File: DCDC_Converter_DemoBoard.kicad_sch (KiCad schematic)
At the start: 90 parts, among them J1 Conn_01x01, J10 Conn_01x01, J11 Conn_01x01, J12 Conn_01x01, J13 Conn_01x01, J14 Conn_01x01, J15 Conn_01x01, J16 Conn_01x01, J17 Conn_01x01, J18 Conn_01x01, J19 Conn_01x01, J2 Conn_01x01, J20 Conn_01x01, J21 Conn_01x01, J22 Conn_01x01, J23 Conn_01x01, J24 Conn_01x01, J3 Conn_01x01, J4 Conn_01x01, J5 Conn_01x01, J6 Conn_01x01, J7 Conn_01x01, J8 Conn_01x01, J9 Conn_01x01

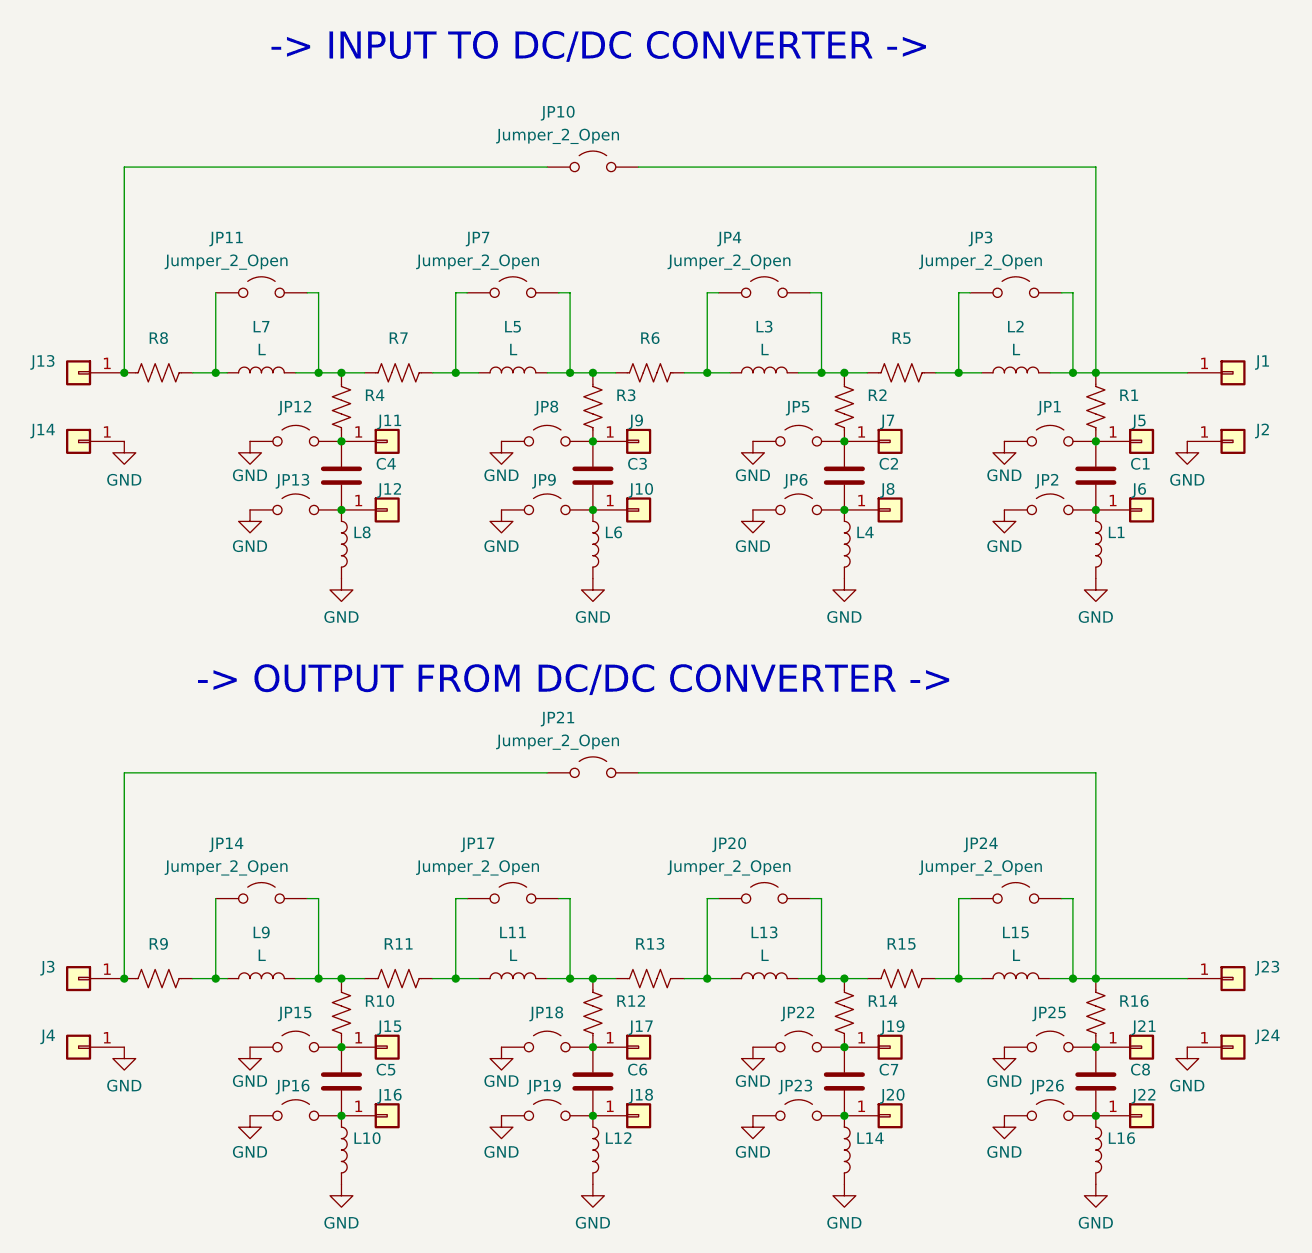
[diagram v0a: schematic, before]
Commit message: completed board layout and exported gerbers
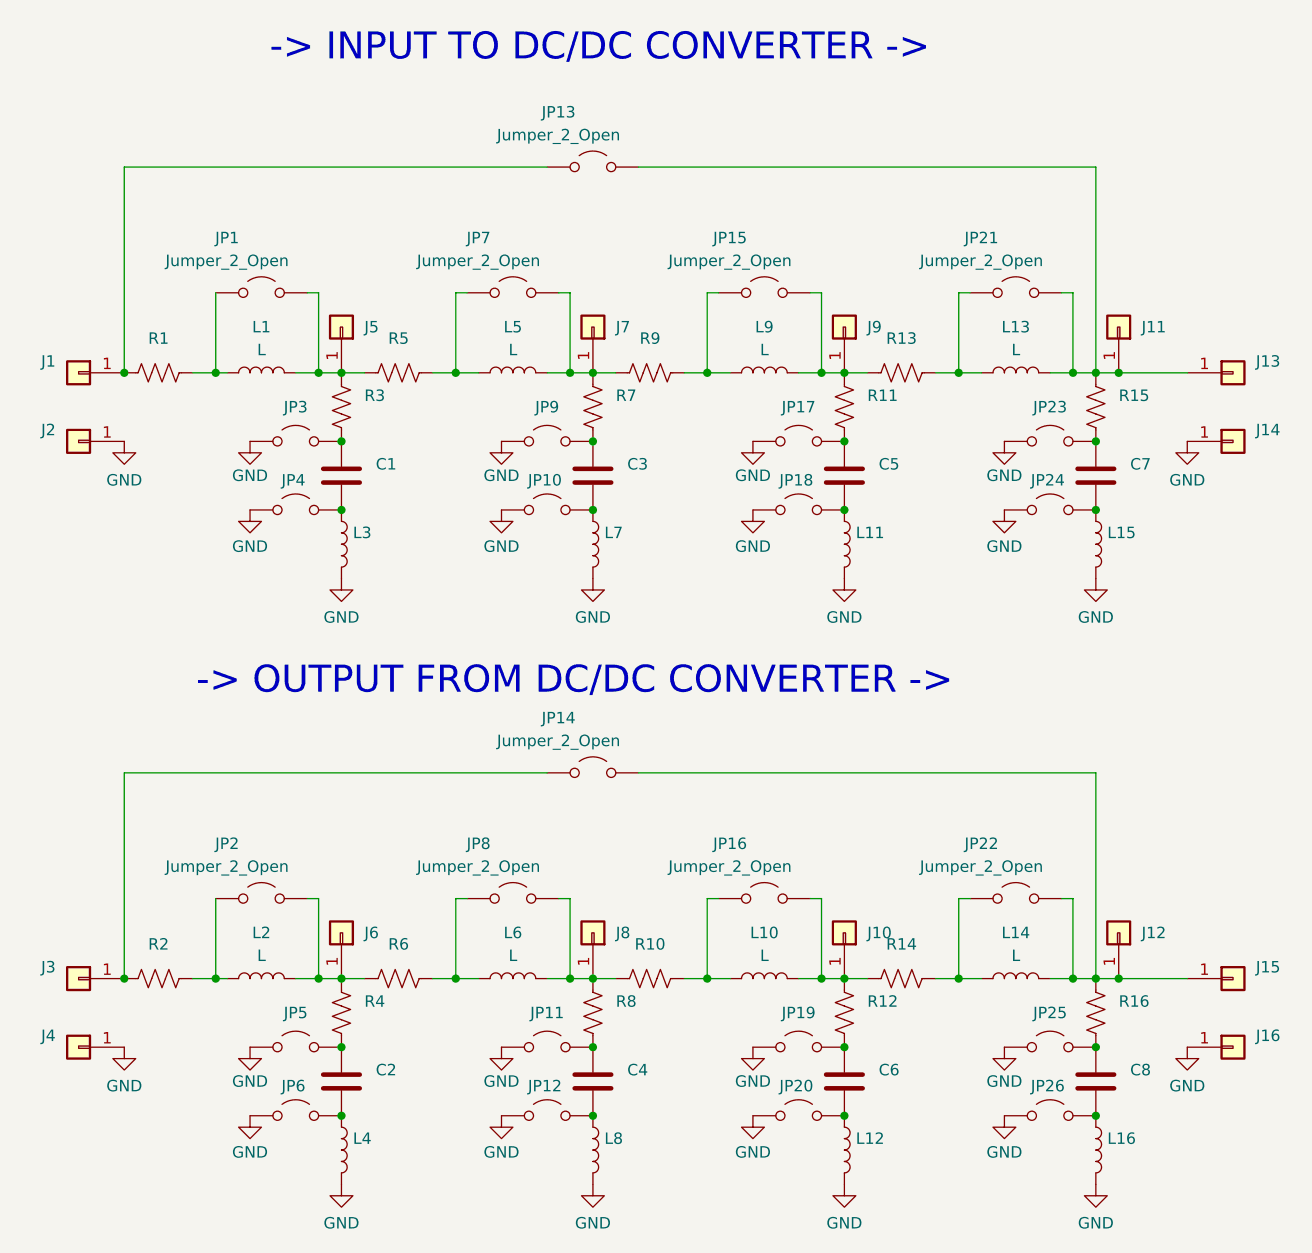
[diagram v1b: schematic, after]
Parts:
- removed J15, J16, J17, J18, J19, J20, J21, J22: Conn_01x01, symbol Connector_Generic:Conn_01x01
- C1: renamed from C4; footprint (none) -> Capacitor_SMD:C_0805_2012Metric_Pad1.18x1.45mm_HandSolder
- C2: renamed from C5; footprint (none) -> Capacitor_SMD:C_0805_2012Metric_Pad1.18x1.45mm_HandSolder
- C3, C8: footprint (none) -> Capacitor_SMD:C_0805_2012Metric_Pad1.18x1.45mm_HandSolder
- C4: renamed from C6; footprint (none) -> Capacitor_SMD:C_0805_2012Metric_Pad1.18x1.45mm_HandSolder
- C5: renamed from C2; footprint (none) -> Capacitor_SMD:C_0805_2012Metric_Pad1.18x1.45mm_HandSolder
- C6: renamed from C7; footprint (none) -> Capacitor_SMD:C_0805_2012Metric_Pad1.18x1.45mm_HandSolder
- C7: renamed from C1; footprint (none) -> Capacitor_SMD:C_0805_2012Metric_Pad1.18x1.45mm_HandSolder
- J1: renamed from J13; footprint (none) -> Connector_PinHeader_2.54mm:PinHeader_1x01_P2.54mm_Vertical
- J10, J11, J12, J3, J4, J5, J6, J7, J8, J9: footprint (none) -> Connector_PinHeader_2.54mm:PinHeader_1x01_P2.54mm_Vertical
- J13: renamed from J1; footprint (none) -> Connector_PinHeader_2.54mm:PinHeader_1x01_P2.54mm_Vertical
- J14: renamed from J2; footprint (none) -> Connector_PinHeader_2.54mm:PinHeader_1x01_P2.54mm_Vertical
- J15: renamed from J23; footprint (none) -> Connector_PinHeader_2.54mm:PinHeader_1x01_P2.54mm_Vertical
- J16: renamed from J24; footprint (none) -> Connector_PinHeader_2.54mm:PinHeader_1x01_P2.54mm_Vertical
- J2: renamed from J14; footprint (none) -> Connector_PinHeader_2.54mm:PinHeader_1x01_P2.54mm_Vertical
- JP1: renamed from JP11; footprint (none) -> Connector_PinHeader_2.54mm:PinHeader_1x02_P2.54mm_Vertical
- JP10: renamed from JP9; footprint (none) -> Connector_PinHeader_2.54mm:PinHeader_1x02_P2.54mm_Vertical
- JP11: renamed from JP18; footprint (none) -> Connector_PinHeader_2.54mm:PinHeader_1x02_P2.54mm_Vertical
- JP12: renamed from JP19; footprint (none) -> Connector_PinHeader_2.54mm:PinHeader_1x02_P2.54mm_Vertical
- JP13: renamed from JP10; footprint (none) -> Connector_PinHeader_2.54mm:PinHeader_1x02_P2.54mm_Vertical
- JP14: renamed from JP21; footprint (none) -> Connector_PinHeader_2.54mm:PinHeader_1x02_P2.54mm_Vertical
- JP15: renamed from JP4; footprint (none) -> Connector_PinHeader_2.54mm:PinHeader_1x02_P2.54mm_Vertical
- JP16: renamed from JP20; footprint (none) -> Connector_PinHeader_2.54mm:PinHeader_1x02_P2.54mm_Vertical
- JP17: renamed from JP5; footprint (none) -> Connector_PinHeader_2.54mm:PinHeader_1x02_P2.54mm_Vertical
- JP18: renamed from JP6; footprint (none) -> Connector_PinHeader_2.54mm:PinHeader_1x02_P2.54mm_Vertical
- JP19: renamed from JP22; footprint (none) -> Connector_PinHeader_2.54mm:PinHeader_1x02_P2.54mm_Vertical
- JP2: renamed from JP14; footprint (none) -> Connector_PinHeader_2.54mm:PinHeader_1x02_P2.54mm_Vertical
- JP20: renamed from JP23; footprint (none) -> Connector_PinHeader_2.54mm:PinHeader_1x02_P2.54mm_Vertical
- JP21: renamed from JP3; footprint (none) -> Connector_PinHeader_2.54mm:PinHeader_1x02_P2.54mm_Vertical
- JP22: renamed from JP24; footprint (none) -> Connector_PinHeader_2.54mm:PinHeader_1x02_P2.54mm_Vertical
- JP23: renamed from JP1; footprint (none) -> Connector_PinHeader_2.54mm:PinHeader_1x02_P2.54mm_Vertical
- JP24: renamed from JP2; footprint (none) -> Connector_PinHeader_2.54mm:PinHeader_1x02_P2.54mm_Vertical
- JP25, JP26, JP7: footprint (none) -> Connector_PinHeader_2.54mm:PinHeader_1x02_P2.54mm_Vertical
- JP3: renamed from JP12; footprint (none) -> Connector_PinHeader_2.54mm:PinHeader_1x02_P2.54mm_Vertical
- JP4: renamed from JP13; footprint (none) -> Connector_PinHeader_2.54mm:PinHeader_1x02_P2.54mm_Vertical
- JP5: renamed from JP15; footprint (none) -> Connector_PinHeader_2.54mm:PinHeader_1x02_P2.54mm_Vertical
- JP6: renamed from JP16; footprint (none) -> Connector_PinHeader_2.54mm:PinHeader_1x02_P2.54mm_Vertical
- JP8: renamed from JP17; footprint (none) -> Connector_PinHeader_2.54mm:PinHeader_1x02_P2.54mm_Vertical
- JP9: renamed from JP8; footprint (none) -> Connector_PinHeader_2.54mm:PinHeader_1x02_P2.54mm_Vertical
- L1: renamed from L7; footprint (none) -> Inductor_SMD:L_10.4x10.4_H4.8
- L10: renamed from L13; footprint (none) -> Inductor_SMD:L_10.4x10.4_H4.8
- L11: renamed from L4; footprint (none) -> Inductor_SMD:L_1812_4532Metric_Pad1.30x3.40mm_HandSolder
- L12: renamed from L14; footprint (none) -> Inductor_SMD:L_1812_4532Metric_Pad1.30x3.40mm_HandSolder
- L13: renamed from L2; footprint (none) -> Inductor_SMD:L_10.4x10.4_H4.8
- L14: renamed from L15; footprint (none) -> Inductor_SMD:L_10.4x10.4_H4.8
- L15: renamed from L1; footprint (none) -> Inductor_SMD:L_1008_2520Metric_Pad1.43x2.20mm_HandSolder
- L16: footprint (none) -> Inductor_SMD:L_1008_2520Metric_Pad1.43x2.20mm_HandSolder
- L2: renamed from L9; footprint (none) -> Inductor_SMD:L_10.4x10.4_H4.8
- L3: renamed from L8; footprint (none) -> Inductor_SMD:L_1812_4532Metric_Pad1.30x3.40mm_HandSolder
- L4: renamed from L10; footprint (none) -> Inductor_SMD:L_1812_4532Metric_Pad1.30x3.40mm_HandSolder
- L5: footprint (none) -> Inductor_SMD:L_10.4x10.4_H4.8
- L6: renamed from L11; footprint (none) -> Inductor_SMD:L_10.4x10.4_H4.8
- L7: renamed from L6; footprint (none) -> Inductor_SMD:L_1812_4532Metric_Pad1.30x3.40mm_HandSolder
- L8: renamed from L12; footprint (none) -> Inductor_SMD:L_1812_4532Metric_Pad1.30x3.40mm_HandSolder
- L9: renamed from L3; footprint (none) -> Inductor_SMD:L_10.4x10.4_H4.8
- R1: renamed from R8; footprint (none) -> Resistor_SMD:R_0805_2012Metric_Pad1.20x1.40mm_HandSolder
- R10: renamed from R13; footprint (none) -> Resistor_SMD:R_0805_2012Metric_Pad1.20x1.40mm_HandSolder
- R11: renamed from R2; footprint (none) -> Resistor_SMD:R_0805_2012Metric_Pad1.20x1.40mm_HandSolder
- R12: renamed from R14; footprint (none) -> Resistor_SMD:R_0805_2012Metric_Pad1.20x1.40mm_HandSolder
- R13: renamed from R5; footprint (none) -> Resistor_SMD:R_0805_2012Metric_Pad1.20x1.40mm_HandSolder
- R14: renamed from R15; footprint (none) -> Resistor_SMD:R_0805_2012Metric_Pad1.20x1.40mm_HandSolder
- R15: renamed from R1; footprint (none) -> Resistor_SMD:R_0805_2012Metric_Pad1.20x1.40mm_HandSolder
- R16: footprint (none) -> Resistor_SMD:R_0805_2012Metric_Pad1.20x1.40mm_HandSolder
- R2: renamed from R9; footprint (none) -> Resistor_SMD:R_0805_2012Metric_Pad1.20x1.40mm_HandSolder
- R3: renamed from R4; footprint (none) -> Resistor_SMD:R_0805_2012Metric_Pad1.20x1.40mm_HandSolder
- R4: renamed from R10; footprint (none) -> Resistor_SMD:R_0805_2012Metric_Pad1.20x1.40mm_HandSolder
- R5: renamed from R7; footprint (none) -> Resistor_SMD:R_0805_2012Metric_Pad1.20x1.40mm_HandSolder
- R6: renamed from R11; footprint (none) -> Resistor_SMD:R_0805_2012Metric_Pad1.20x1.40mm_HandSolder
- R7: renamed from R3; footprint (none) -> Resistor_SMD:R_0805_2012Metric_Pad1.20x1.40mm_HandSolder
- R8: renamed from R12; footprint (none) -> Resistor_SMD:R_0805_2012Metric_Pad1.20x1.40mm_HandSolder
- R9: renamed from R6; footprint (none) -> Resistor_SMD:R_0805_2012Metric_Pad1.20x1.40mm_HandSolder
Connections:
- net at J15.1 (Pin_1), JP14.2 (B), JP22.2 (B)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: now also J12.1 (Pin_1)
- net at JP16.2 (B), L10.2, R12.1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: now also J10.1 (Pin_1)
- net at JP1.2 (B), L1.2, R3.1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: now also J5.1 (Pin_1)
- net at JP8.2 (B), L6.2, R10.1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: now also J8.1 (Pin_1)
- net at JP2.2 (B), L2.2, R4.1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: now also J6.1 (Pin_1)
- net at J13.1 (Pin_1), JP13.2 (B), JP21.2 (B)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: now also J11.1 (Pin_1)
- net at C7.1, JP23.2 (B), R15.2: no longer J5.1 (Pin_1)
- net at C3.1, JP9.2 (B), R7.2: no longer J9.1 (Pin_1)
- net at C1.2, JP4.2 (B), L3.1: no longer J12.1 (Pin_1)
- net at JP7.2 (B), L5.2, R7.1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: now also J7.1 (Pin_1)
- net at C7.2, JP24.2 (B), L15.1: no longer J6.1 (Pin_1)
- net at C5.1, JP17.2 (B), R11.2: no longer J7.1 (Pin_1)
- net at C5.2, JP18.2 (B), L11.1: no longer J8.1 (Pin_1)
- net at C1.1, JP3.2 (B), R3.2: no longer J11.1 (Pin_1)
- net at JP15.2 (B), L9.2, R11.1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: now also J9.1 (Pin_1)
- net at C3.2, JP10.2 (B), L7.1: no longer J10.1 (Pin_1)

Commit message: fixed footprint and cleaned up silkscreen
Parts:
- L15, L16: footprint Inductor_SMD:L_1008_2520Metric_Pad1.43x2.20mm_HandSolder -> Inductor_SMD:L_1812_4532Metric_Pad1.30x3.40mm_HandSolder
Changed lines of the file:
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@@
 			)
 		)
-		(property "Footprint" "Inductor_SMD:L_1008_2520Metric_Pad1.43x2.20mm_HandSolder"
+		(property "Footprint" "Inductor_SMD:L_1812_4532Metric_Pad1.30x3.40mm_HandSolder"
 			(at 194.31 142.24 0)
 			(effects
@@
 			)
 		)
-		(property "Footprint" "Inductor_SMD:L_1008_2520Metric_Pad1.43x2.20mm_HandSolder"
+		(property "Footprint" "Inductor_SMD:L_1812_4532Metric_Pad1.30x3.40mm_HandSolder"
 			(at 194.31 74.93 0)
 			(effects
